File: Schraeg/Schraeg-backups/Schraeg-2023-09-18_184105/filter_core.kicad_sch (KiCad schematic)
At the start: 38 parts

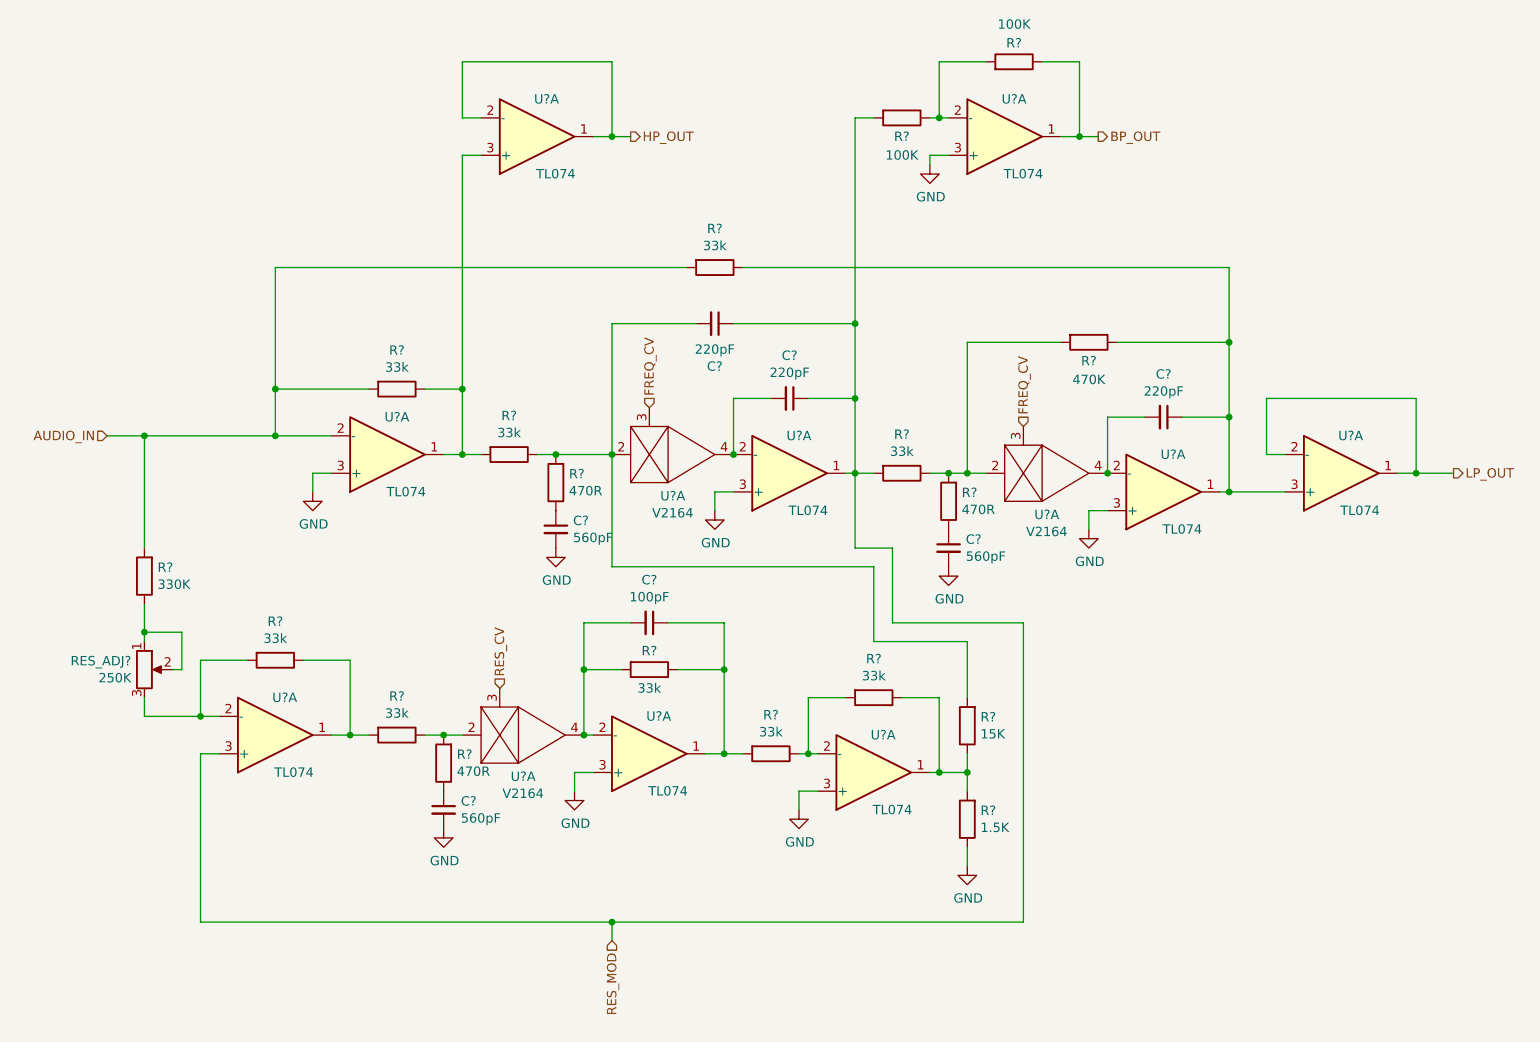
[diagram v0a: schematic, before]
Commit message: fixes filter schematic
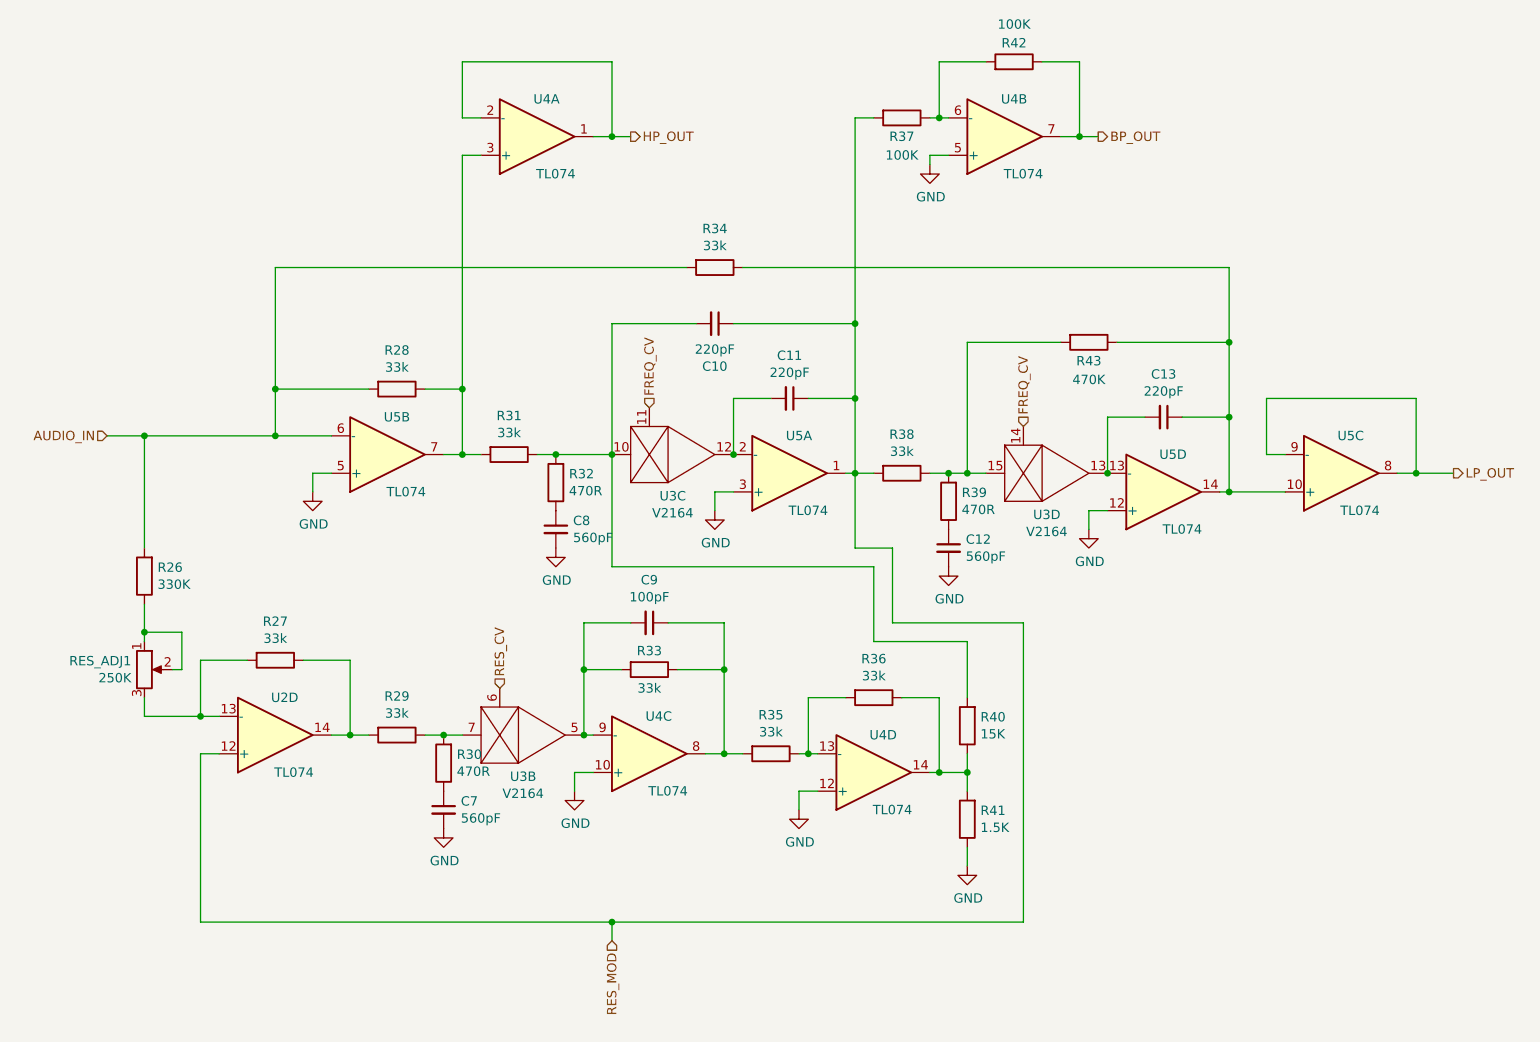
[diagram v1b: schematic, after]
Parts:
- gave numbers to parts that had none: 30
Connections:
- net AUDIO_IN: now also U5.6 (-); no longer U5.2 (-)
- net BP_OUT: now also U4.7; no longer U4.1
- net FREQ_CV: now also U3.11, U3.14; no longer U3.3, U3.3
- net GND: now also U4.10 (+), U4.12 (+), U4.5 (+), U5.12 (+), U5.5 (+); no longer U4.3 (+), U4.3 (+), U4.3 (+), U5.3 (+), U5.3 (+)
- net LP_OUT: now also U5.8, U5.9 (-); no longer U5.1, U5.2 (-)
- net RES_CV: now also U3.6; no longer U3.3
- net RES_MOD: now also U2.12 (+); no longer U2.3 (+)
- net at R28.1, R31.2, U4.3 (+): now also U5.7; no longer U5.1
- net at R27.1, R29.2: now also U2.14; no longer U2.1
- net at R27.2, RES_ADJ1.3: now also U2.13 (-); no longer U2.2 (-)
- net at C11.2, U5.2 (-): now also U3.12; no longer U3.4
- net at R37.1, R42.2: now also U4.6 (-); no longer U4.2 (-)
- net at C13.1, R34.1, R43.1: now also U5.10 (+), U5.14; no longer U5.1, U5.3 (+)
- net at C9.1, R33.1, R35.2: now also U4.8; no longer U4.1
- net at C9.2, R33.2: now also U3.5, U4.9 (-); no longer U3.4, U4.2 (-)
- net at R36.1, R40.1, R41.2: now also U4.14; no longer U4.1
- net at R35.1, R36.2: now also U4.13 (-); no longer U4.2 (-)
- net at C10.2, R31.1, R32.2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: now also U3.10; no longer U3.2
- net at R38.1, R39.2, R43.2: now also U3.15; no longer U3.2
- net at R29.1, R30.2: now also U3.7; no longer U3.2
- new net: C13.2, U3.13, U5.13 (-)
